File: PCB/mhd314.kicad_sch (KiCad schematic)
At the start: 35 parts, among them J1 Raspberry_Pi_2_3, J2 AudioJack_Pentaconn, J4 AudioJack3_SwitchTR, SW1 SW_Push

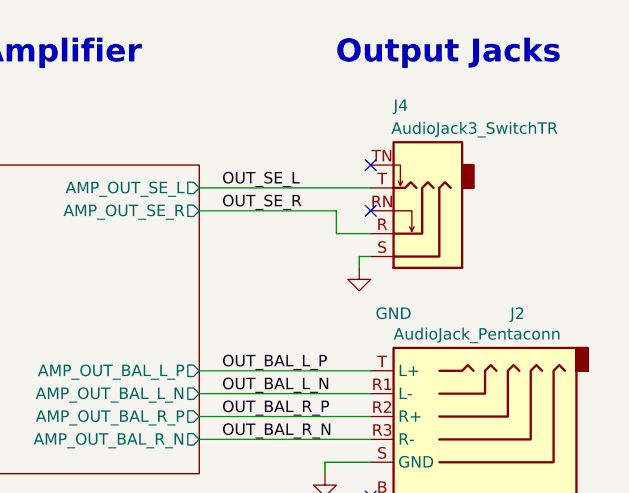
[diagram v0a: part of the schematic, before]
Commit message: Changed single ended connector for gold plated part and changed resistor and capacitor values of opa1622 amp for improved power on high impedance headphones
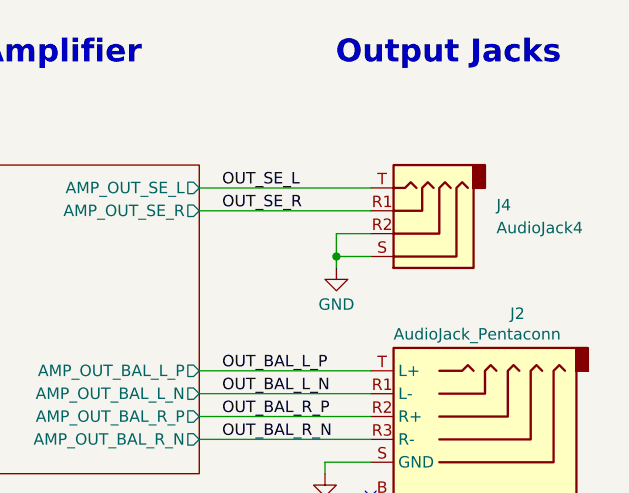
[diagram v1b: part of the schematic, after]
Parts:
- removed J4: AudioJack3_SwitchTR, Connector_Audio:Jack_3.5mm_CUI_SJ1-3535NG_Horizontal, symbol Connector_Audio:AudioJack3_SwitchTR
- added J4: AudioJack4, mahaudio KiCad Library:TENSILITY_54-00176, symbol Connector_Audio:AudioJack4
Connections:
- net GND: now also J4.R2, J4.S
- net OUT_SE_L: now also J4.T
- net OUT_SE_R: now also J4.R1
- no-connect marks 22 -> 20
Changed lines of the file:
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@@
 		(color 0 0 0 0)
 	)
-	(no_connect
-		(at 171.45 58.42)
+	(junction
+		(at 250.19 54.61)
+		(diameter 0)
+		(color 0 0 0 0)
 	)
 	(no_connect
-		(at 254 49.53)
+		(at 171.45 58.42)
 	)
 	(no_connect
@@
 		(at 36.83 97.79)
 	)
-	(no_connect
-		(at 254 44.45)
-	)
 	(wire
 		(pts
@@
 	(wire
 		(pts
+			(xy 250.19 54.61) (xy 254 54.61)
+		)
+		(stroke
+			(width 0)
+			(type default)
+		)
+	)
+	(wire
+		(pts
+			(xy 254 52.07) (xy 250.19 52.07)
+		)
+		(stroke
+			(width 0)
+			(type default)
+		)
+	)
+	(wire
+		(pts
 			(xy 158.75 128.27) (xy 175.26 128.27)
 		)
@@
 	(wire
 		(pts
-			(xy 252.73 54.61) (xy 252.73 55.88)
+			(xy 250.19 54.61) (xy 250.19 55.88)
 		)
 		(stroke
@@
 	(wire
 		(pts
-			(xy 250.19 49.53) (xy 250.19 52.07)
-		)
-		(stroke
-			(width 0)
-			(type default)
-		)
-	)
-	(wire
-		(pts
 			(xy 77.47 69.85) (xy 133.35 69.85)
 		)
@@
 	(wire
 		(pts
-			(xy 234.95 49.53) (xy 250.19 49.53)
+			(xy 234.95 49.53) (xy 254 49.53)
 		)
 		(stroke
@@
 	(wire
 		(pts
+			(xy 250.19 52.07) (xy 250.19 54.61)
+		)
+		(stroke
+			(width 0)
+			(type default)
+		)
+	)
+	(wire
+		(pts
 			(xy 158.75 135.89) (xy 175.26 135.89)
 		)
@@
 	(wire
 		(pts
-			(xy 250.19 52.07) (xy 254 52.07)
-		)
-		(stroke
-			(width 0)
-			(type default)
-		)
-	)
-	(wire
-		(pts
 			(xy 171.45 49.53) (xy 191.77 49.53)
 		)
@@
 	(wire
 		(pts
-			(xy 252.73 54.61) (xy 254 54.61)
-		)
-		(stroke
-			(width 0)
-			(type default)
-		)
-	)
-	(wire
-		(pts
 			(xy 97.79 130.81) (xy 97.79 134.62)
 		)
@@
 	)
 	(symbol
-		(lib_id "Connector_Audio:AudioJack3_SwitchTR")
-		(at 259.08 52.07 180)
-		(unit 1)
-		(exclude_from_sim no)
-		(in_bom yes)
-		(on_board yes)
-		(dnp no)
-		(property "Reference" "J4"
-			(at 256.54 37.846 0)
-			(effects
-				(font
-					(size 1.27 1.27)
-				)
-				(justify right)
-			)
-		)
-		(property "Value" "AudioJack3_SwitchTR"
-			(at 256.286 40.386 0)
-			(effects
-				(font
-					(size 1.27 1.27)
-				)
-				(justify right)
-			)
-		)
-		(property "Footprint" "Connector_Audio:Jack_3.5mm_CUI_SJ1-3535NG_Horizontal"
-			(at 259.08 52.07 0)
-			(effects
-				(font
-					(size 1.27 1.27)
-				)
-				(hide yes)
-			)
-		)
-		(property "Datasheet" "https://www.sameskydevices.com/product/resource/sj1-353xng.pdf"
-			(at 259.08 52.07 0)
-			(effects
-				(font
-					(size 1.27 1.27)
-				)
-				(hide yes)
-			)
-		)
-		(property "Description" "Audio Jack, 3 Poles (Stereo / TRS), Switched TR Poles (Normalling)"
-			(at 259.08 52.07 0)
-			(effects
-				(font
-					(size 1.27 1.27)
-				)
-				(hide yes)
-			)
-		)
-		(property "JLCPCB Part #" "C22359743"
-			(at 259.08 52.07 0)
-			(effects
-				(font
-					(size 1.27 1.27)
-				)
-				(hide yes)
-			)
-		)
-		(pin "RN"
-		)
-		(pin "S"
-		)
-		(pin "T"
-		)
-		(pin "TN"
-		)
-		(pin "R"
-		)
-		(instances
-			(project ""
-				(path "/afee45fc-2361-4efb-9cde-757fc2efd57b"
-					(reference "J4")
-					(unit 1)
-				)
-			)
-		)
-	)
-	(symbol
 		(lib_id "Switch:SW_Push")
 		(at 119.38 116.84 270)
@@
 	(symbol
 		(lib_id "power:GND")
-		(at 252.73 55.88 0)
+		(at 250.19 55.88 0)
 		(unit 1)
 		(exclude_from_sim no)
@@
 		(dnp no)
 		(property "Reference" "#PWR085"
-			(at 252.73 62.23 0)
+			(at 250.19 62.23 0)
 			(effects
 				(font
@@
 		)
 		(property "Value" "GND"
-			(at 256.54 60.96 0)
+			(at 250.19 59.944 0)
 			(effects
 				(font
@@
 		)
 		(property "Footprint" ""
-			(at 252.73 55.88 0)
+			(at 250.19 55.88 0)
 			(effects
 				(font
@@
 		)
 		(property "Datasheet" ""
-			(at 252.73 55.88 0)
+			(at 250.19 55.88 0)
 			(effects
 				(font
@@
 		)
 		(property "Description" "Power symbol creates a global label with name \"GND\" , ground"
-			(at 252.73 55.88 0)
+			(at 250.19 55.88 0)
 			(effects
 				(font
@@
 					(unit 1)
 				)
+			)
+		)
+	)
+	(symbol
+		(lib_id "Connector_Audio:AudioJack4")
+		(at 259.08 52.07 180)
+		(unit 1)
+		(exclude_from_sim no)
+		(in_bom yes)
+		(on_board yes)
+		(dnp no)
+		(fields_autoplaced yes)
+		(property "Reference" "J4"
+			(at 267.97 48.8949 0)
+			(effects
+				(font
+					(size 1.27 1.27)
+				)
+				(justify right)
+			)
+		)
+		(property "Value" "AudioJack4"
+			(at 267.97 51.4349 0)
+			(effects
+				(font
+					(size 1.27 1.27)
+				)
+				(justify right)
+			)
+		)
+		(property "Footprint" "mahaudio KiCad Library:TENSILITY_54-00176"
+			(at 259.08 52.07 0)
+			(effects
+				(font
+					(size 1.27 1.27)
+				)
+				(hide yes)
+			)
+		)
+		(property "Datasheet" "~"
+			(at 259.08 52.07 0)
+			(effects
+				(font
+					(size 1.27 1.27)
+				)
+				(hide yes)
+			)
+		)
+		(property "Description" "Audio Jack, 4 Poles (TRRS)"
+			(at 259.08 52.07 0)
+			(effects
+				(font
+					(size 1.27 1.27)
+				)
+				(hide yes)
+			)
+		)
+		(property "JLCPCB Part #" "C19857277"
+			(at 259.08 52.07 0)
+			(effects
+				(font
+					(size 1.27 1.27)
+				)
+				(hide yes)
+			)
+		)
+		(pin "R2"
+		)
+		(pin "S"
+		)
+		(pin "T"
+		)
+		(pin "R1"
+		)
+		(instances
+			(project ""
+				(path "/afee45fc-2361-4efb-9cde-757fc2efd57b"
+					(reference "J4")
+					(unit 1)
+				)

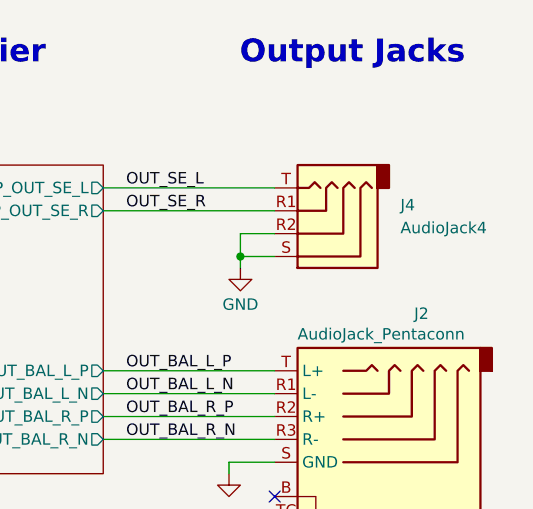
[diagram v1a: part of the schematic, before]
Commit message: Changes in E2P for better identification of the board
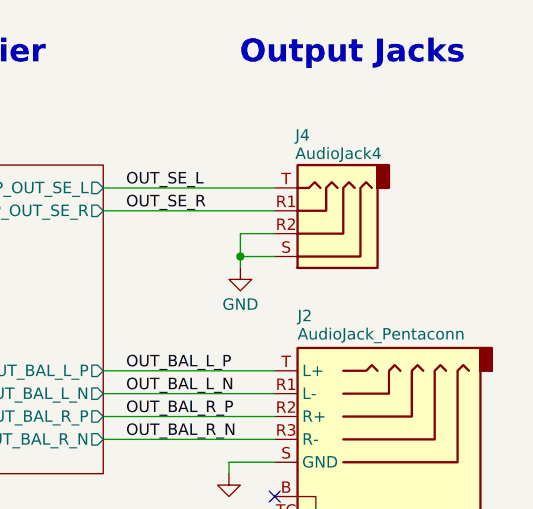
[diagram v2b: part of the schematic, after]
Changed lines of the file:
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@@
 		(on_board yes)
 		(dnp no)
-		(fields_autoplaced yes)
 		(property "Reference" "J4"
-			(at 267.97 48.8949 0)
+			(at 256.286 41.148 0)
 			(effects
 				(font
@@
 		)
 		(property "Value" "AudioJack4"
-			(at 267.97 51.4349 0)
+			(at 256.286 43.18 0)
 			(effects
 				(font
@@
 		(dnp no)
 		(property "Reference" "J2"
-			(at 269.494 60.96 0)
-			(effects
-				(font
+			(at 256.54 61.214 0)
+			(effects
+				(font
